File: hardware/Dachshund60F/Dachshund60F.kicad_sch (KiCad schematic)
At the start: 207 parts, among them J1 USB daughterboard (JST-SH 4P), J2 Battery (JST-PH 2P), J3 SWD, J4 Display, Q1 AO3401A, SW1 Power, SW100 MX Esc (1.00u), SW101 MX F1 (1.00u), SW102 MX F2 (1.00u), SW103 MX F3 (1.00u), SW104 MX F4 (1.00u), SW105 MX F5 (1.00u), SW106 MX F6 (1.00u), SW107 MX F7 (1.00u), SW108 MX F8 (1.00u), SW109 MX F9 (1.00u), SW110 MX F10 (1.00u), SW111 MX F11 (1.00u), SW112 MX F12 (1.00u), SW113 MX Delete (1.00u), SW2 Reset, SW200 MX ` (1.00u), SW201 MX 1 (1.00u), SW202 MX 2 (1.00u), SW203 MX 3 (1.00u), SW204 MX 4 (1.00u), SW205 MX 5 (1.00u), SW206 MX 6 (1.00u), SW207 MX 7 (1.00u), SW208 MX 8 (1.00u), SW209 MX 9 (1.00u), SW210 MX 0 (1.00u), SW211 MX - (1.00u), SW212 MX = (1.00u), SW213 MX Backspace (2.00u), SW3 PEC12R-4220F-S0024 (horizonta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, SW300 MX Tab (1.50u), SW301 MX Q (1.00u), SW302 MX W (1.00u), SW303 MX E (1.00u), SW304 MX R (1.00u), SW305 MX T (1.00u), SW306 MX Y (1.00u), SW307 MX U (1.00u), SW308 MX I (1.00u), SW309 MX O (1.00u), SW310 MX P (1.00u), SW311 MX [ (1.00u), SW312 MX ] (1.00u), SW313 MX \ (1.50u), SW400 MX Caps Lock (1.75u), SW401 MX A (1.00u), SW402 MX S (1.00u), SW403 MX D (1.00u), SW404 MX F (1.00u), SW405 MX G (1.00u), SW406 MX H (1.00u), SW407 MX J (1.00u), SW408 MX K (1.00u), SW409 MX L (1.00u), SW410 MX ; (1.00u), SW411 MX ' (1.00u), SW413 MX Enter (2.25u), SW500 MX Shift (2.25u), SW501 MX Z (1.00u), SW502 MX X (1.00u), SW503 MX C (1.00u), SW504 MX V (1.00u), SW505 MX B (1.00u), SW506 MX N (1.00u), SW507 MX M (1.00u), SW508 MX , (1.00u), SW509 MX . (1.00u), SW510 MX / (1.00u), SW512 MX Shift (1.75u), SW513 MX Up (1.00u), SW600 MX Ctrl (1.25u), SW601 MX Win (1.25u), SW603 MX Alt (1.25u), SW604 MX Mod (1.25u, solder)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

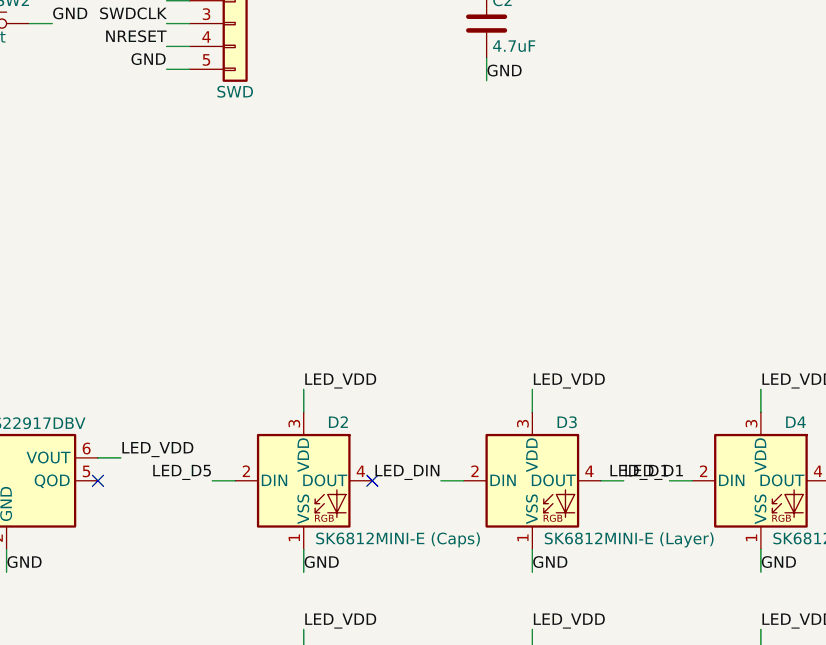
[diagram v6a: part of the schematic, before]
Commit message: Buffer the LED data line for the higher USB-side LED_VDD
With the power path, LED_VDD is about 4.7 V on USB, which puts the
SK6812 input-high threshold (0.7 x VDD) at the 3.3 V data level. U4, an
SN74LV1T34 with TTL-level inputs powered from LED_VDD, now drives D3's
DIN (net LED_DIN_BUF), decoupled by C19. Placed on the back above D3.
ERC and DRC show no new errors.

Co-Authored-By: Claude Opus 5.5 (1M context) <noreply@anthropic.com>
Claude-Session: https://claude.ai/code/session_01D9WgQVzjyM3BLJSpari9iy
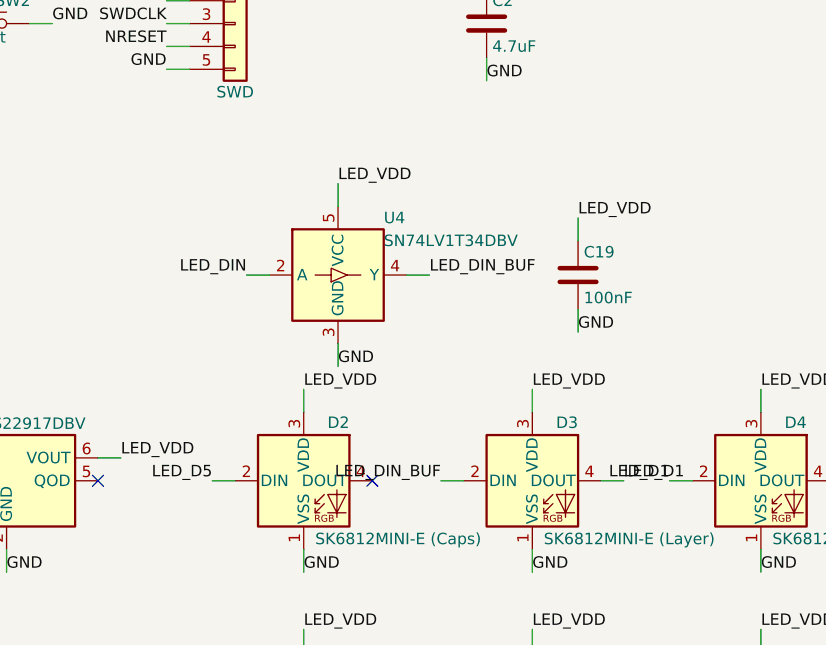
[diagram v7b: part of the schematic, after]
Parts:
- added C19: 100nF, Capacitor_SMD:C_0402_1005Metric, symbol Device:C
- added U4: SN74LV1T34DBV, Package_TO_SOT_SMD:SOT-23-5, symbol Logic_LevelTranslator:SN74LV1T34DBV
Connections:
- net GND: now also C19.2, U4.3 (GND)
- net LED_DIN: now also U4.2 (A); no longer D3.2 (DIN)
- net LED_VDD: now also C19.1, U4.5 (VCC)
- new net LED_DIN_BUF: D3.2 (DIN), U4.4 (Y)
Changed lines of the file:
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@@
 		)
 	)
-	(label "LED_DIN"
+	(label "LED_DIN_BUF"
 		(at 142.24 330.2 180)
 		(effects
@@
 		(effects
 			(font
+				(size 1.27 1.27)
+			)
+			(justify left bottom)
+		)
+	)
+	(symbol
+		(lib_id "Logic_LevelTranslator:SN74LV1T34DBV")
+		(at 130.81 307.34 0)
+		(unit 1)
+		(in_bom yes)
+		(on_board yes)
+		(dnp no)
+		(property "Reference" "U4"
+			(at 135.89000000000001 300.98999999999995 0)
+			(effects
+				(font
+					(size 1.27 1.27)
+				)
+				(justify left)
+			)
+		)
+		(property "Value" "SN74LV1T34DBV"
+			(at 135.89000000000001 303.53 0)
+			(effects
+				(font
+					(size 1.27 1.27)
+				)
+				(justify left)
+			)
+		)
+		(property "Footprint" "Package_TO_SOT_SMD:SOT-23-5"
+			(at 130.81 307.34 0)
+			(hide yes)
+			(effects
+				(font
+					(size 1.27 1.27)
+				)
+			)
+		)
+		(property "Datasheet" "https://www.ti.com/lit/ds/symlink/sn74lv1t34.pdf"
+			(at 130.81 307.34 0)
+			(hide yes)
+			(effects
+				(font
+					(size 1.27 1.27)
+				)
+			)
+		)
+		(property "Description" "LED data buffer: TTL-level input, so 3.3 V logic drives the SK6812s at any LED_VDD"
+			(at 130.81 307.34 0)
+			(hide yes)
+			(effects
+				(font
+					(size 1.27 1.27)
+				)
+			)
+		)
+		(instances
+			(project "Dachshund60F"
+				(path "/1d3f02fb-327d-4e90-8f04-7e58052bd7d3"
+					(reference "U4")
+					(unit 1)
+				)
+			)
+		)
+	)
+	(wire
+		(pts
+			(xy 123.19 307.34) (xy 120.65 307.34)
+		)
+		(stroke
+			(width 0)
+			(type default)
+		)
+	)
+	(label "LED_DIN"
+		(at 120.65 307.34 180)
+		(effects
+			(font
+				(size 1.27 1.27)
+			)
+			(justify right bottom)
+		)
+	)
+	(wire
+		(pts
+			(xy 138.43 307.34) (xy 140.97 307.34)
+		)
+		(stroke
+			(width 0)
+			(type default)
+		)
+	)
+	(label "LED_DIN_BUF"
+		(at 140.97 307.34 0)
+		(effects
+			(font
+				(size 1.27 1.27)
+			)
+			(justify left bottom)
+		)
+	)
+	(wire
+		(pts
+			(xy 130.81 299.71999999999997) (xy 130.81 297.17999999999995)
+		)
+		(stroke
+			(width 0)
+			(type default)
+		)
+	)
+	(label "LED_VDD"
+		(at 130.81 297.17999999999995 0)
+		(effects
+			(font
+				(size 1.27 1.27)
+			)
+			(justify left bottom)
+		)
+	)
+	(wire
+		(pts
+			(xy 130.81 314.96) (xy 130.81 317.5)
+		)
+		(stroke
+			(width 0)
+			(type default)
+		)
+	)
+	(label "GND"
+		(at 130.81 317.5 0)
+		(effects
+			(font
+				(size 1.27 1.27)
+			)
+			(justify left bottom)
+		)
+	)
+	(symbol
+		(lib_id "Device:C")
+		(at 157.48 307.34 0)
+		(unit 1)
+		(in_bom yes)
+		(on_board yes)
+		(dnp no)
+		(property "Reference" "C19"
+			(at 158.11499999999998 304.79999999999995 0)
+			(effects
+				(font
+					(size 1.27 1.27)
+				)
+				(justify left)
+			)
+		)
+		(property "Value" "100nF"
+			(at 158.11499999999998 309.88 0)
+			(effects
+				(font
+					(size 1.27 1.27)
+				)
+				(justify left)
+			)
+		)
+		(property "Footprint" "Capacitor_SMD:C_0402_1005Metric"
+			(at 157.48 307.34 0)
+			(hide yes)
+			(effects
+				(font
+					(size 1.27 1.27)
+				)
+			)
+		)
+		(property "Datasheet" ""
+			(at 157.48 307.34 0)
+			(hide yes)
+			(effects
+				(font
+					(size 1.27 1.27)
+				)
+			)
+		)
+		(property "Description" "Unpolarized capacitor"
+			(at 157.48 307.34 0)
+			(hide yes)
+			(effects
+				(font
+					(size 1.27 1.27)
+				)
+			)
+		)
+		(instances
+			(project "Dachshund60F"
+				(path "/1d3f02fb-327d-4e90-8f04-7e58052bd7d3"
+					(reference "C19")
+					(unit 1)
+				)
+			)
+		)
+	)
+	(wire
+		(pts
+			(xy 157.48 303.53) (xy 157.48 300.98999999999995)
+		)
+		(stroke
+			(width 0)
+			(type default)
+		)
+	)
+	(label "LED_VDD"
+		(at 157.48 300.98999999999995 0)
+		(effects
+			(font
+				(size 1.27 1.27)
+			)
+			(justify left bottom)
+		)
+	)
+	(wire
+		(pts
+			(xy 157.48 311.15) (xy 157.48 313.69)
+		)
+		(stroke
+			(width 0)
+			(type default)
+		)
+	)
+	(label "GND"
+		(at 157.48 313.69 0)
+		(effects
+			(font

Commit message: Add test pads for probing the mainboard
Nine 1.5 mm SMD test pads on the back, each on its net's existing
track with the net name on the silkscreen: VBUS, VBAT, VBAT_SW, VSYS,
+3V3, LED_VDD, CHG_STAT and two GND. Excluded from the BOM. DRC and ERC
show no new errors or warnings. The bring-up plan lists where each is.

Co-Authored-By: Claude Opus 5.5 (1M context) <noreply@anthropic.com>
Claude-Session: https://claude.ai/code/session_01D9WgQVzjyM3BLJSpari9iy
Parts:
- added TP1: VBUS, TestPoint:TestPoint_Pad_D1.5mm, symbol Connector:TestPoint
- added TP2: VBAT, TestPoint:TestPoint_Pad_D1.5mm, symbol Connector:TestPoint
- added TP3: VBAT_SW, TestPoint:TestPoint_Pad_D1.5mm, symbol Connector:TestPoint
- added TP4: VSYS, TestPoint:TestPoint_Pad_D1.5mm, symbol Connector:TestPoint
- added TP5: +3V3, TestPoint:TestPoint_Pad_D1.5mm, symbol Connector:TestPoint
- added TP6: LED_VDD, TestPoint:TestPoint_Pad_D1.5mm, symbol Connector:TestPoint
- added TP7: CHG_STAT, TestPoint:TestPoint_Pad_D1.5mm, symbol Connector:TestPoint
- added TP8, TP9: GND, TestPoint:TestPoint_Pad_D1.5mm, symbol Connector:TestPoint
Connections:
- net +3V3: now also TP5.1
- net CHG_STAT: now also TP7.1
- net GND: now also TP8.1, TP9.1
- net LED_VDD: now also TP6.1
- net VBAT: now also TP2.1
- net VBAT_SW: now also TP3.1
- net VBUS: now also TP1.1
- net VSYS: now also TP4.1
